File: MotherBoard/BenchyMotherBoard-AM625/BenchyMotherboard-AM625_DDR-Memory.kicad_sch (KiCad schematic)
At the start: 39 parts, among them U1 AM6254ATCGGAALW, U19 MT40A1G16TB-062E:F

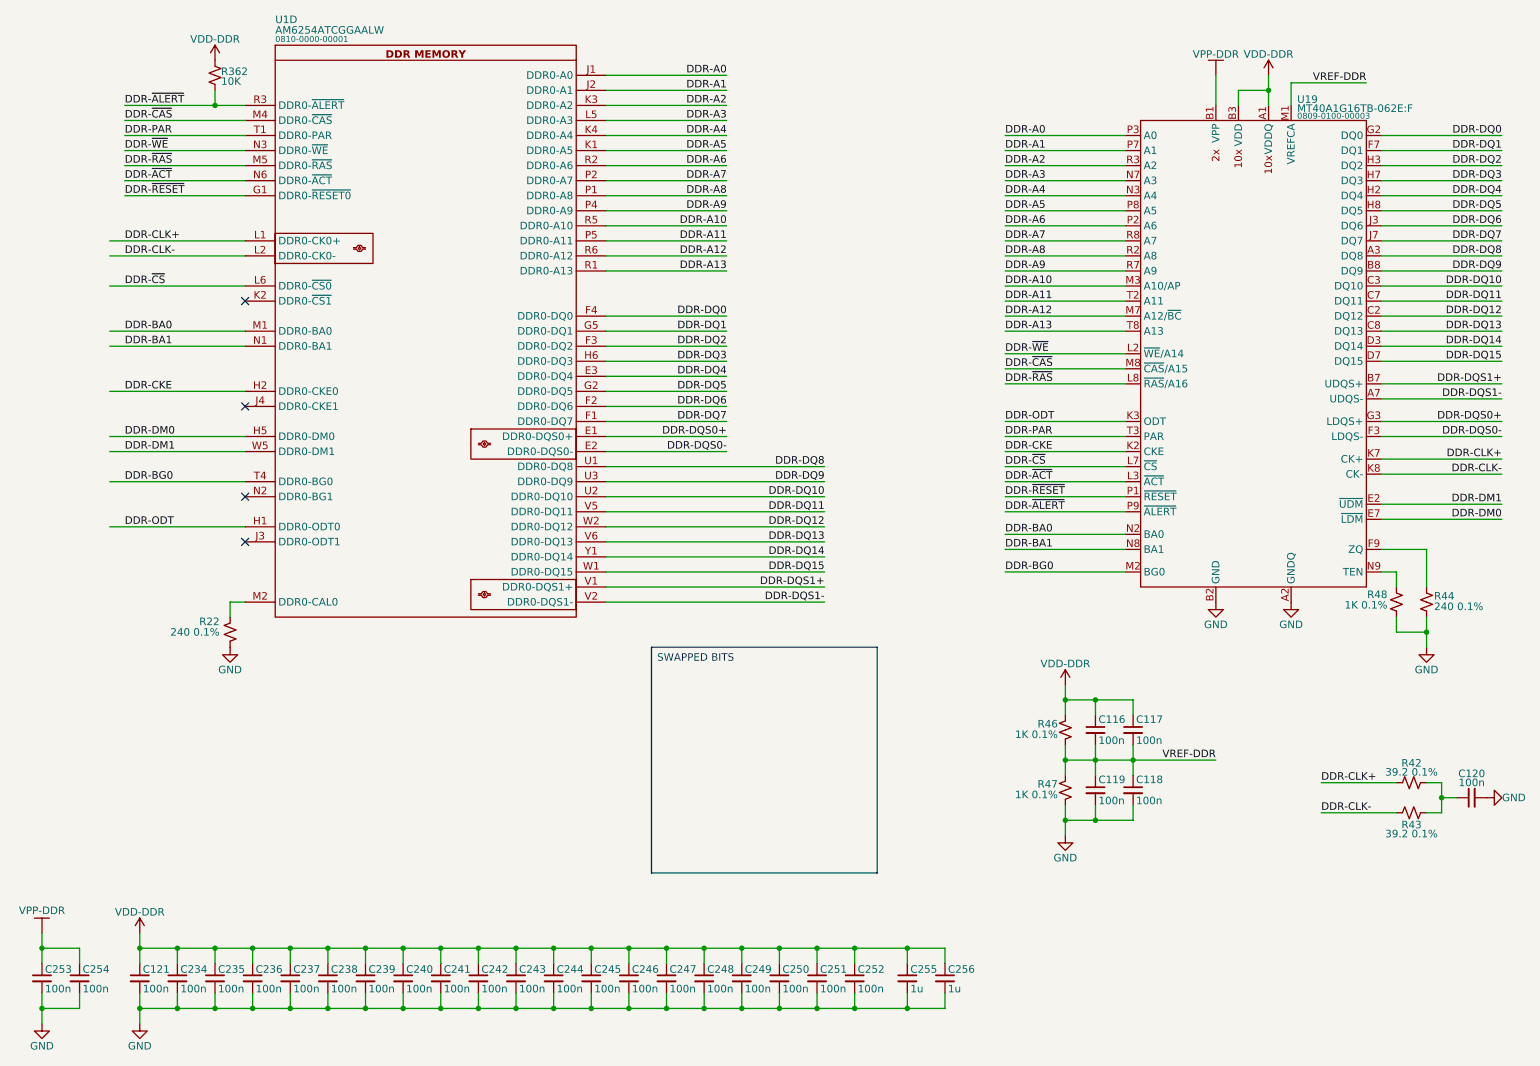
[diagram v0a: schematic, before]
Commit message: Schematic capture mostly complete. Starting PCB layout
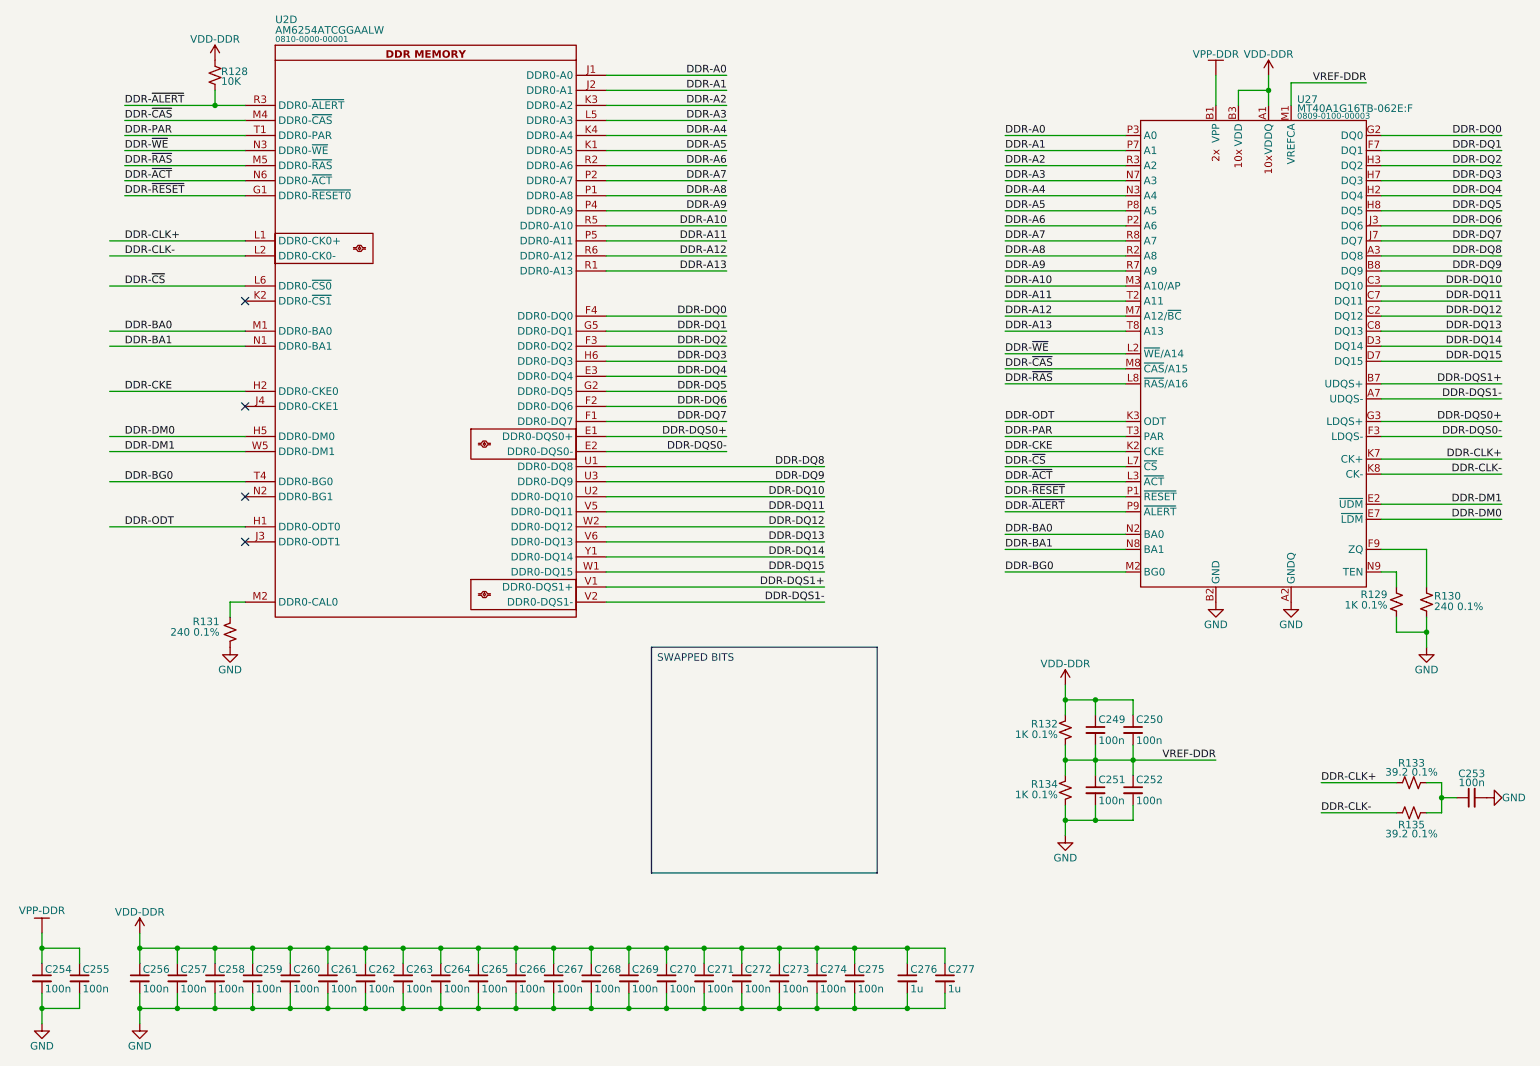
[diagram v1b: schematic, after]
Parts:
- renumbered C116 to C249, C117 to C250, C119 to C251, C118 to C252, C120 to C253, C253 to C254, C254 to C255, C121 to C256, C234 to C257, C235 to C258, C236 to C259, C237 to C260, C238 to C261, C239 to C262, C240 to C263, C241 to C264, C242 to C265, C243 to C266, C244 to C267, C245 to C268, C246 to C269, C247 to C270, C248 to C271, C249 to C272, C250 to C273, C251 to C274, C252 to C275, C255 to C276, C256 to C277, R362 to R128, R48 to R129, R44 to R130, R22 to R131, R46 to R132, R42 to R133, R47 to R134, R43 to R135, U1 to U2, U19 to U27
